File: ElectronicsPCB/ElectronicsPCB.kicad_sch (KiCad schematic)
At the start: 16 parts

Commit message: resolved all erc checker issues
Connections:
- no-connect marks 26 -> 28

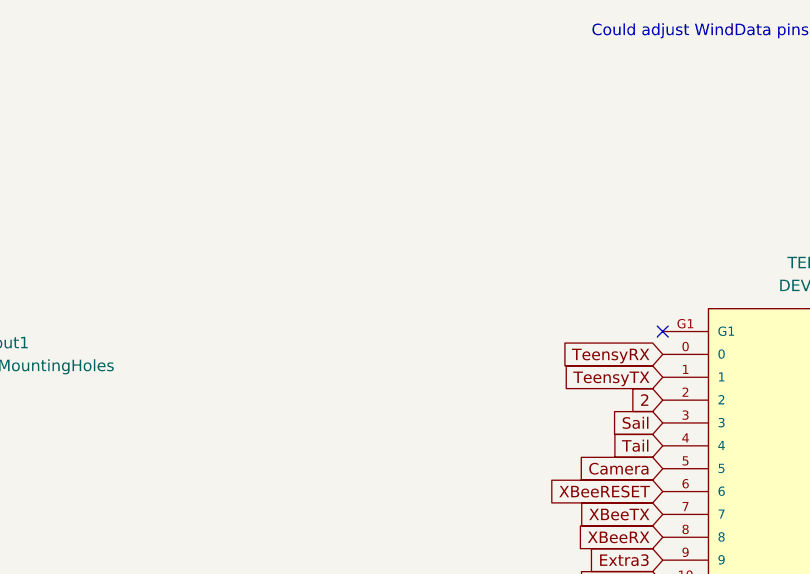
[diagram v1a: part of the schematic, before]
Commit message: added mounting holes
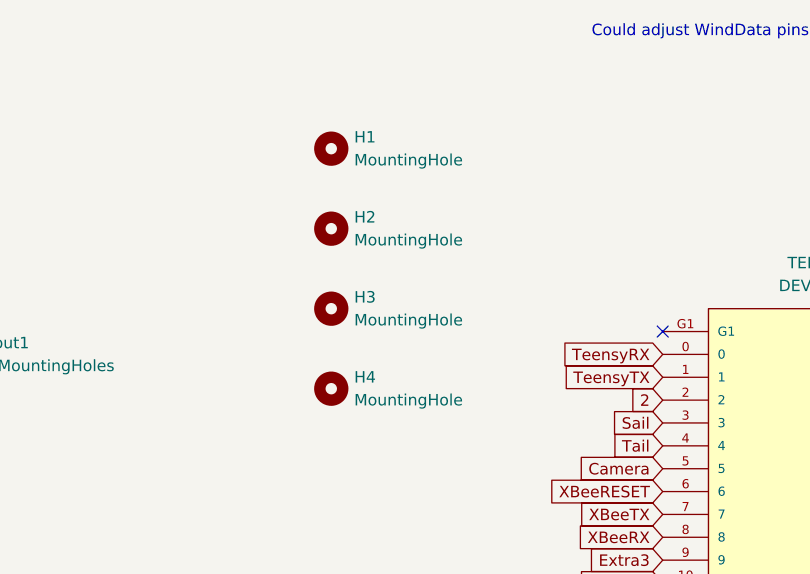
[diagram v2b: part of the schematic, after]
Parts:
- added H1, H2, H3, H4: MountingHole, MountingHole:MountingHole_2.7mm, symbol Mechanical:MountingHole

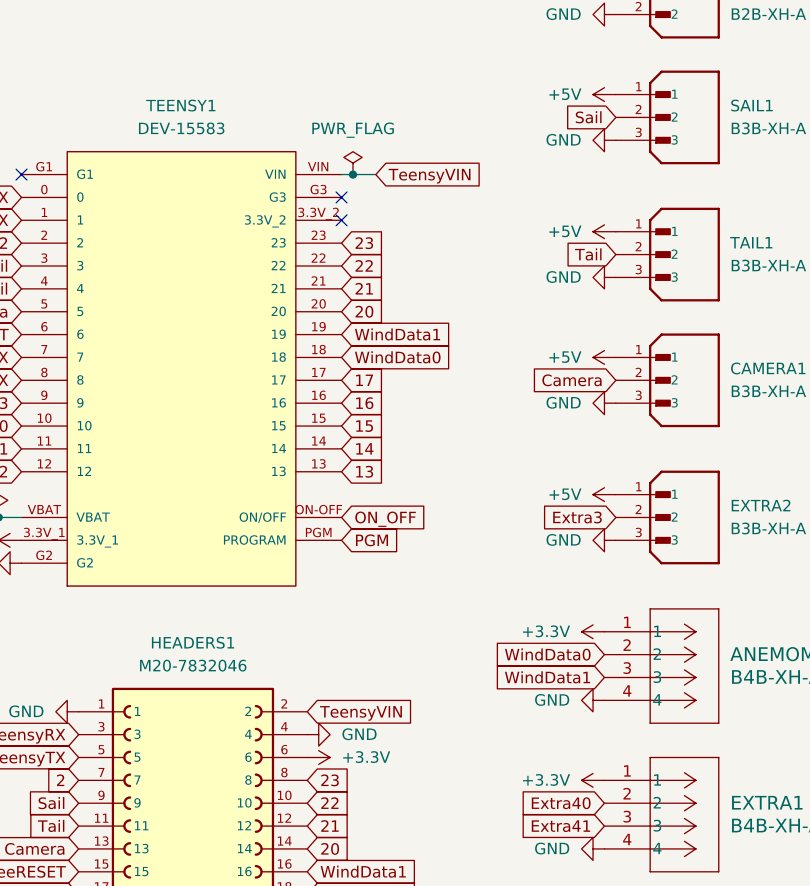
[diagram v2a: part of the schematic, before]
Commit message: fixed teensy power on electronics PCB
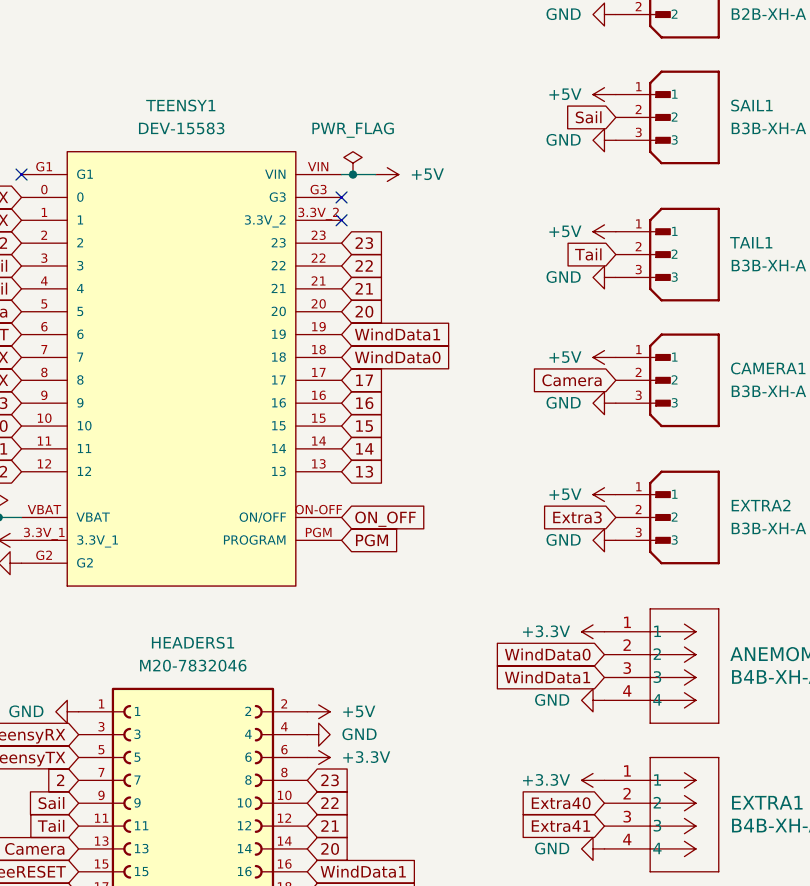
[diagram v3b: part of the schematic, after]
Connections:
- net TeensyVIN is gone; now on net +5V: HEADERS1.2, TEENSY1.VIN
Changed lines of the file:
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@@
 		)
 	)
-	(global_label "TeensyVIN"
-		(shape input)
-		(at 222.25 109.22 0)
-		(fields_autoplaced yes)
-		(effects
-			(font
-				(size 1.27 1.27)
-			)
-			(justify left)
-		)
-		(property "Intersheetrefs" "${INTERSHEET_REFS}"
-			(at 234.5486 109.22 0)
-			(effects
-				(font
-					(size 1.27 1.27)
-				)
-				(justify left)
-				(hide yes)
-			)
-		)
-	)
 	(global_label "23"
 		(shape input)
@@
 		)
 	)
-	(global_label "TeensyVIN"
-		(shape input)
-		(at 229.87 49.53 0)
-		(fields_autoplaced yes)
-		(effects
-			(font
-				(size 1.27 1.27)
-			)
-			(justify left)
-		)
-		(property "Intersheetrefs" "${INTERSHEET_REFS}"
-			(at 242.1686 49.53 0)
-			(effects
-				(font
-					(size 1.27 1.27)
-				)
-				(justify left)
-				(hide yes)
-			)
-		)
-	)
 	(global_label "TeensyTX"
 		(shape input)
@@
 	)
 	(symbol
+		(lib_id "power:+24V")
+		(at 222.25 109.22 270)
+		(unit 1)
+		(exclude_from_sim no)
+		(in_bom yes)
+		(on_board yes)
+		(dnp no)
+		(fields_autoplaced yes)
+		(property "Reference" "#PWR033"
+			(at 218.44 109.22 0)
+			(effects
+				(font
+					(size 1.27 1.27)
+				)
+				(hide yes)
+			)
+		)
+		(property "Value" "+5V"
+			(at 226.06 109.2199 90)
+			(effects
+				(font
+					(size 1.27 1.27)
+				)
+				(justify left)
+			)
+		)
+		(property "Footprint" ""
+			(at 222.25 109.22 0)
+			(effects
+				(font
+					(size 1.27 1.27)
+				)
+				(hide yes)
+			)
+		)
+		(property "Datasheet" ""
+			(at 222.25 109.22 0)
+			(effects
+				(font
+					(size 1.27 1.27)
+				)
+				(hide yes)
+			)
+		)
+		(property "Description" "Power symbol creates a global label with name \"+24V\""
+			(at 222.25 109.22 0)
+			(effects
+				(font
+					(size 1.27 1.27)
+				)
+				(hide yes)
+			)
+		)
+		(pin "1"
+		)
+		(instances
+			(project "ElectronicsPCB"
+				(path "/986f98f1-de62-46c2-9c6e-8a3d3d9a8a4d"
+					(reference "#PWR033")
+					(unit 1)
+				)
+			)
+		)
+	)
+	(symbol
 		(lib_id "power:GND")
 		(at 256.54 90.17 270)
@@
 					(unit 1)
 				)
+			)
+		)
+	)
+	(symbol
+		(lib_id "power:+24V")
+		(at 229.87 49.53 270)
+		(unit 1)
+		(exclude_from_sim no)
+		(in_bom yes)
+		(on_board yes)
+		(dnp no)
+		(fields_autoplaced yes)
+		(property "Reference" "#PWR032"
+			(at 226.06 49.53 0)
+			(effects
+				(font
+					(size 1.27 1.27)
+				)
+				(hide yes)
+			)
+		)
+		(property "Value" "+5V"
+			(at 233.68 49.5299 90)
+			(effects
+				(font
+					(size 1.27 1.27)
+				)
+				(justify left)
+			)
+		)
+		(property "Footprint" ""
+			(at 229.87 49.53 0)
+			(effects
+				(font
+					(size 1.27 1.27)
+				)
+				(hide yes)
+			)
+		)
+		(property "Datasheet" ""
+			(at 229.87 49.53 0)
+			(effects
+				(font
+					(size 1.27 1.27)
+				)
+				(hide yes)
+			)
+		)
+		(property "Description" "Power symbol creates a global label with name \"+24V\""
+			(at 229.87 49.53 0)
+			(effects
+				(font
+					(size 1.27 1.27)
+				)
+				(hide yes)
+			)
+		)
+		(pin "1"
+		)
+		(instances
+			(project "ElectronicsPCB"
+				(path "/986f98f1-de62-46c2-9c6e-8a3d3d9a8a4d"
+					(reference "#PWR032")
+					(unit 1)
+				)

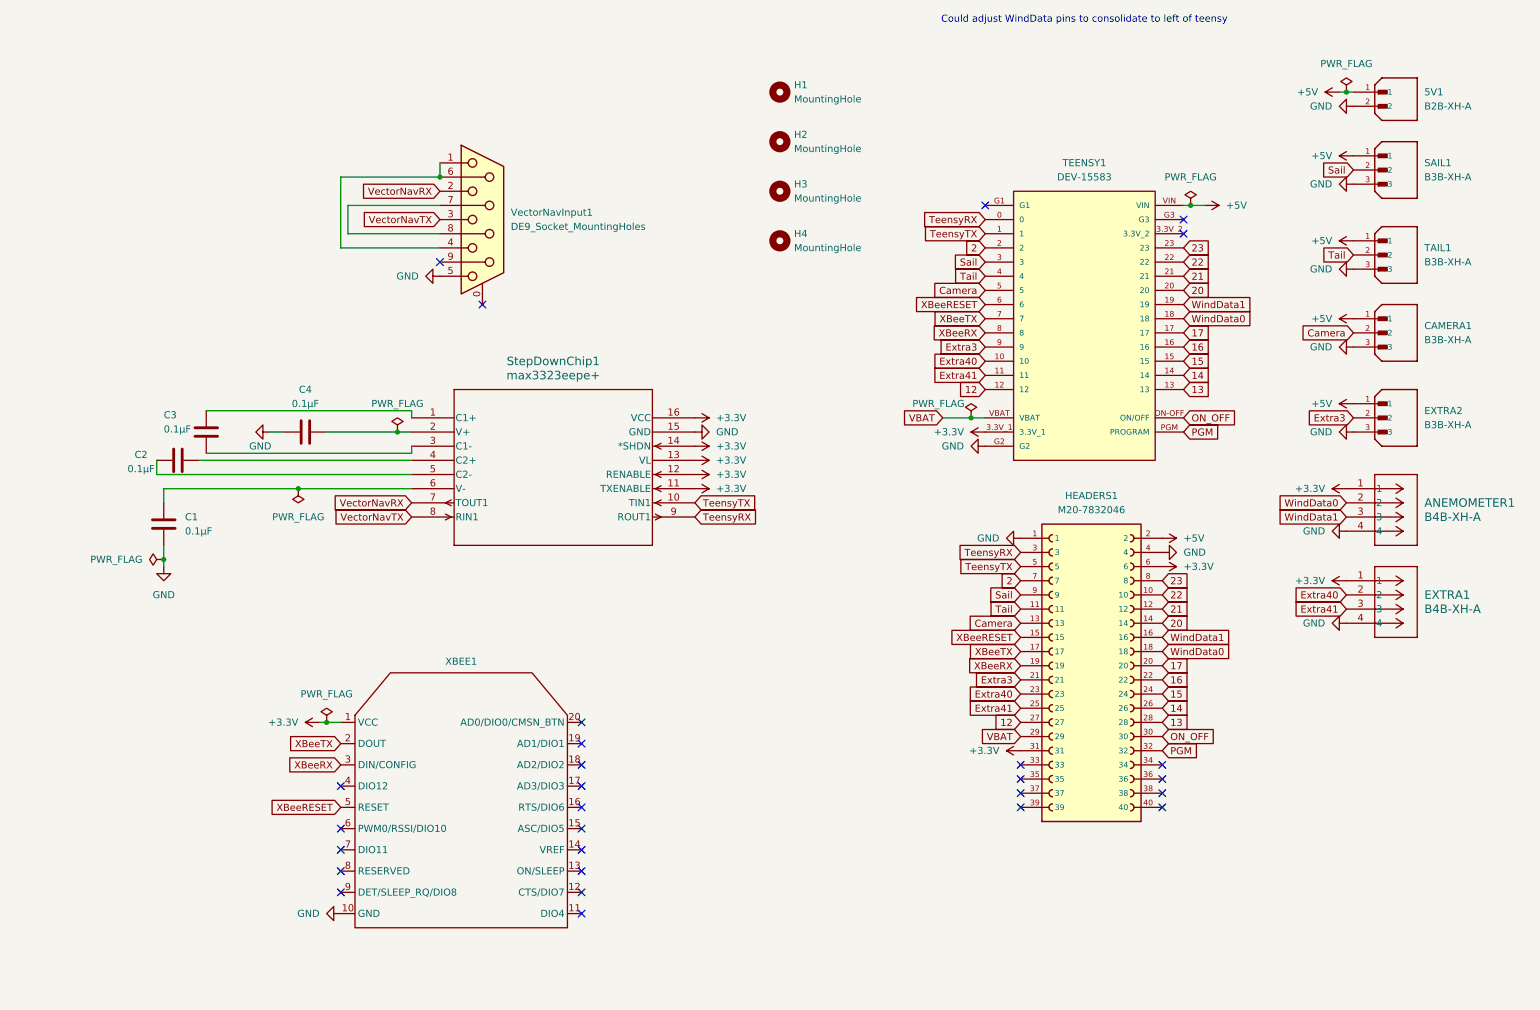
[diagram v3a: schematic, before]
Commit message: overhauled controls pcb
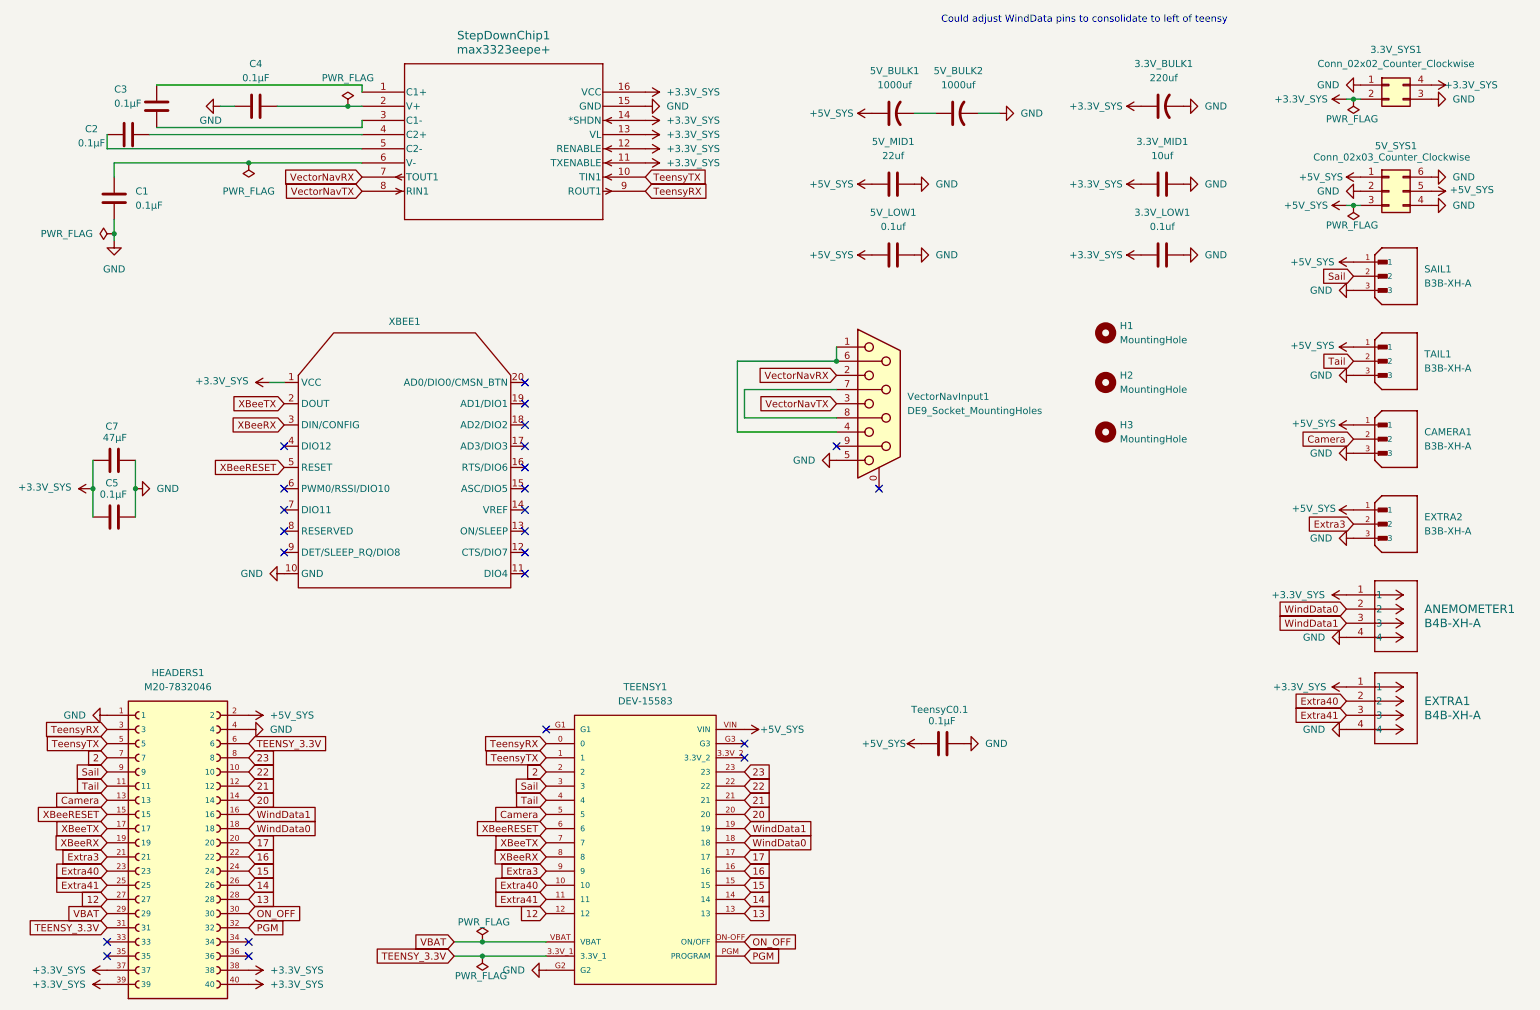
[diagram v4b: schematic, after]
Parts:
- removed 5V1: B2B-XH-A, ElectronicsFootprints:B2B-XH-A, symbol 2-PinConnector:B2B-XH-A
- removed H4: MountingHole, MountingHole:MountingHole_2.7mm, symbol Mechanical:MountingHole
- added 3.3V_BULK1: 220uf, ElectronicsFootprints:CAP_87510_220uf, symbol Device:C_US
- added 3.3V_LOW1, 5V_LOW1: 0.1uf, ElectronicsFootprints:CAP_CL10B_01uf_0603, symbol Device:C
- added 3.3V_MID1: 10uf, ElectronicsFootprints:CAP_CL21A_10uf_0805, symbol Device:C
- added 3.3V_SYS1: Conn_02x02_Counter_Clockwise, Connector_Molex:Molex_Mini-Fit_Jr_5566-04A_2x02_P4.20mm_Vertical, symbol Connector_Generic:Conn_02x02_Counter_Clockwise
- added 5V_BULK1, 5V_BULK2: 1000uf, ElectronicsFootprints:CAP_EEE1A_1000uf, symbol Device:C_US
- added 5V_MID1: 22uf, ElectronicsFootprints:CAP_CL32A_22uf_1210, symbol Device:C
- added 5V_SYS1: Conn_02x03_Counter_Clockwise, Connector_Molex:Molex_Mini-Fit_Jr_5566-06A_2x03_P4.20mm_Vertical, symbol Connector_Generic:Conn_02x03_Counter_Clockwise
- added C5, TeensyC0.1: 0.1µF, ElectronicsFootprints:CAP_CL10B_01uf_0603, symbol Device:C
- added C7: 47µF, ElectronicsFootprints:CAP_C3225_47uf_1210, symbol Device:C
- C1, C2, C3, C4: footprint ElectronicsFootprints:C0402C104K4RACTU_0.1µF -> ElectronicsFootprints:CAP_CL10B_01uf_0603
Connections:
- net GND: now also 3.3V_BULK1.2, 3.3V_LOW1.2, 3.3V_MID1.2, 3.3V_SYS1.1 (Pin_1), 3.3V_SYS1.3 (Pin_3), 5V_BULK2.2, 5V_LOW1.2, 5V_MID1.2, 5V_SYS1.2 (Pin_2), 5V_SYS1.4 (Pin_4), 5V_SYS1.6 (Pin_6), C5.2, C7.2, TeensyC0.1.2
- net +3.3V_SYS: now reaches HEADERS1.37
- net +3.3V_SYS: now also ANEMOMETER1.1, EXTRA1.1, HEADERS1.38, HEADERS1.39, HEADERS1.40, StepDownChip1.11 (TXENABLE), StepDownChip1.12 (RENABLE), StepDownChip1.13 (VL), StepDownChip1.14 (*SHDN), StepDownChip1.16 (VCC), XBEE1.1 (VCC), 3.3V_BULK1.1, 3.3V_LOW1.1, 3.3V_MID1.1, 3.3V_SYS1.2 (Pin_2), 3.3V_SYS1.4 (Pin_4), C5.1, C7.1
- removed net +3.3V: ANEMOMETER1.1, EXTRA1.1, HEADERS1.31, HEADERS1.6, StepDownChip1.11 (TXENABLE), StepDownChip1.12 (RENABLE), StepDownChip1.13 (VL), StepDownChip1.14 (*SHDN), StepDownChip1.16 (VCC), TEENSY1.3.3V_1, XBEE1.1 (VCC)
- net +5V renamed +5V_SYS
- net +5V_SYS: now also 5V_BULK1.1, 5V_LOW1.1, 5V_MID1.1, 5V_SYS1.1 (Pin_1), 5V_SYS1.3 (Pin_3), 5V_SYS1.5 (Pin_5), TeensyC0.1.1
- new net: 5V_BULK1.2, 5V_BULK2.1
- new net TEENSY_3.3V: HEADERS1.31, HEADERS1.6, TEENSY1.3.3V_1
- no-connect marks 28 -> 24
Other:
- moved on the sheet: ANEMOMETER1, C1, C2, C3, C4, CAMERA1, EXTRA1, EXTRA2, H1, H2, H3, HEADERS1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
